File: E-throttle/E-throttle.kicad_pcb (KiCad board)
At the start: 2 copper layers, 100 x 100 mm, 49 parts, among them IC1 BTS441TG, J1 Micro_SD_Card_Det1, J3 Conn_01x11, J4 Conn_01x11, J5 776087-1, Q1 NMOS, SW1 SW_Push, U1 74HC123, U2 LM317_SOT-223, U3 LM317_SOT-223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

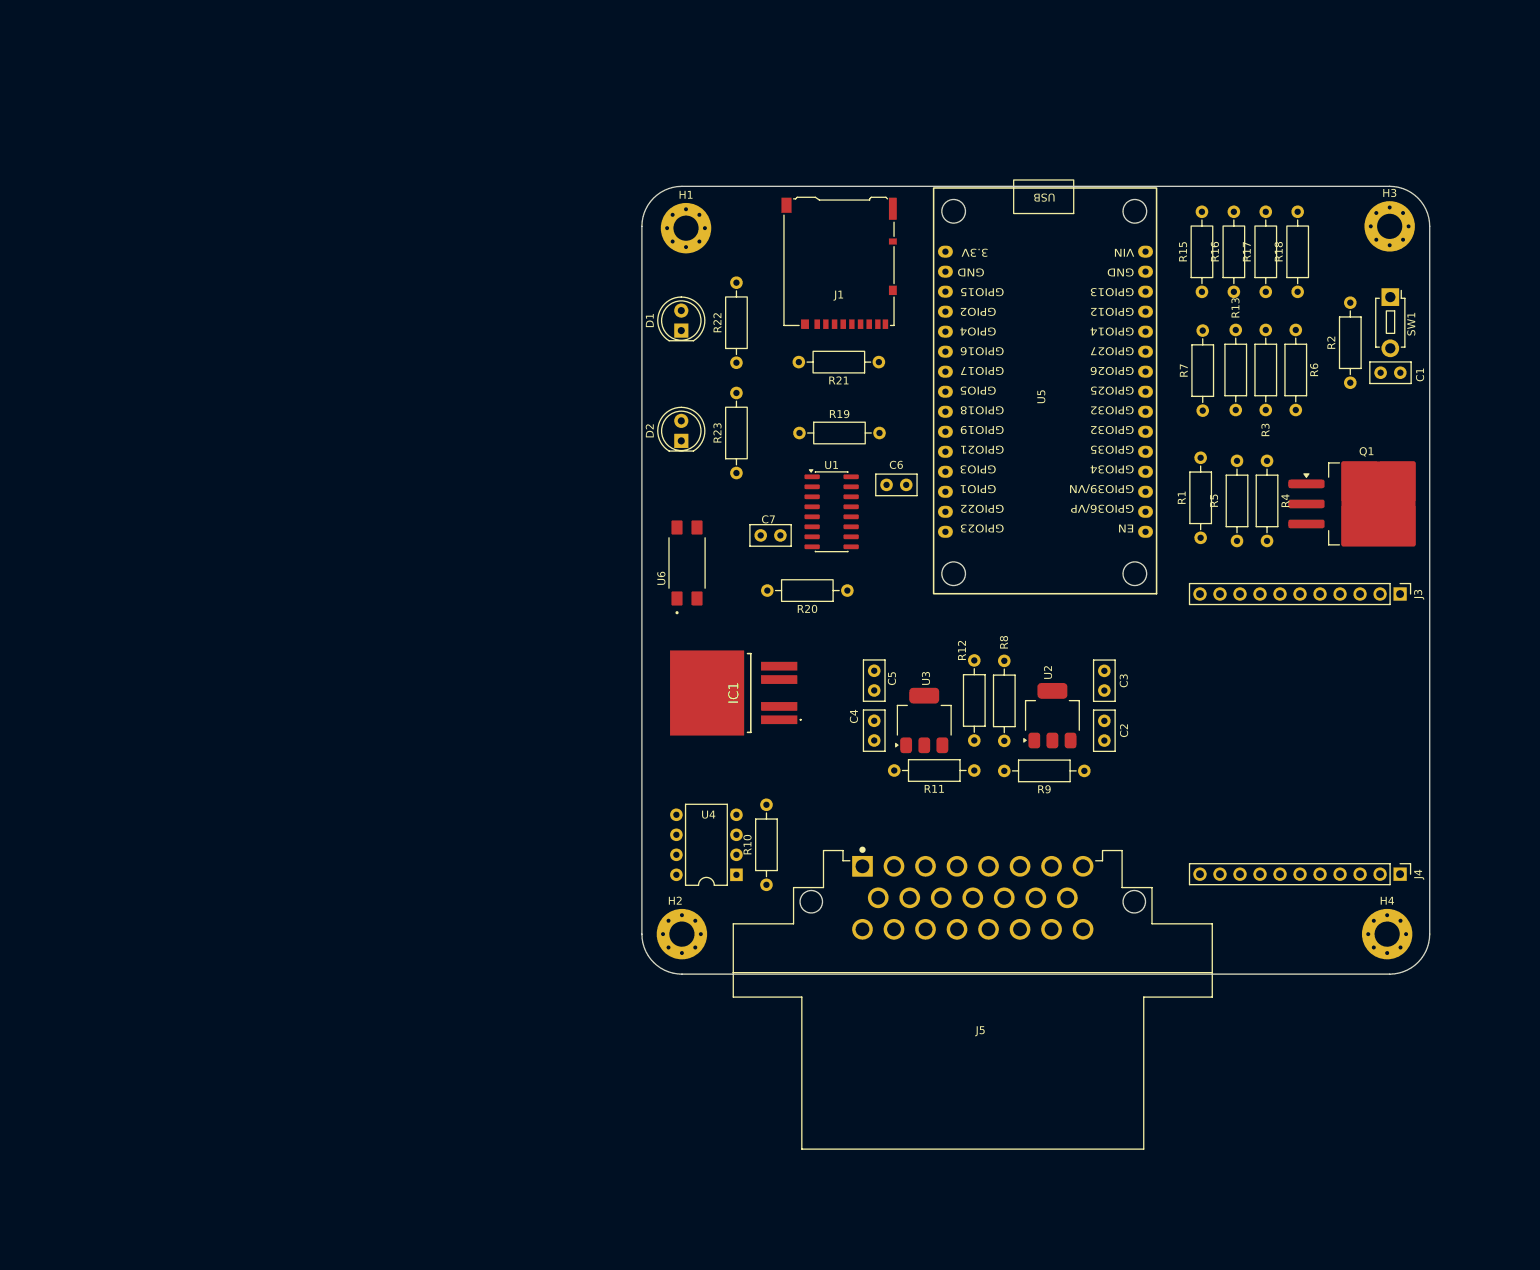
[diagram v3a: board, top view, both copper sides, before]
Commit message: Adjusted layout, added ground plane
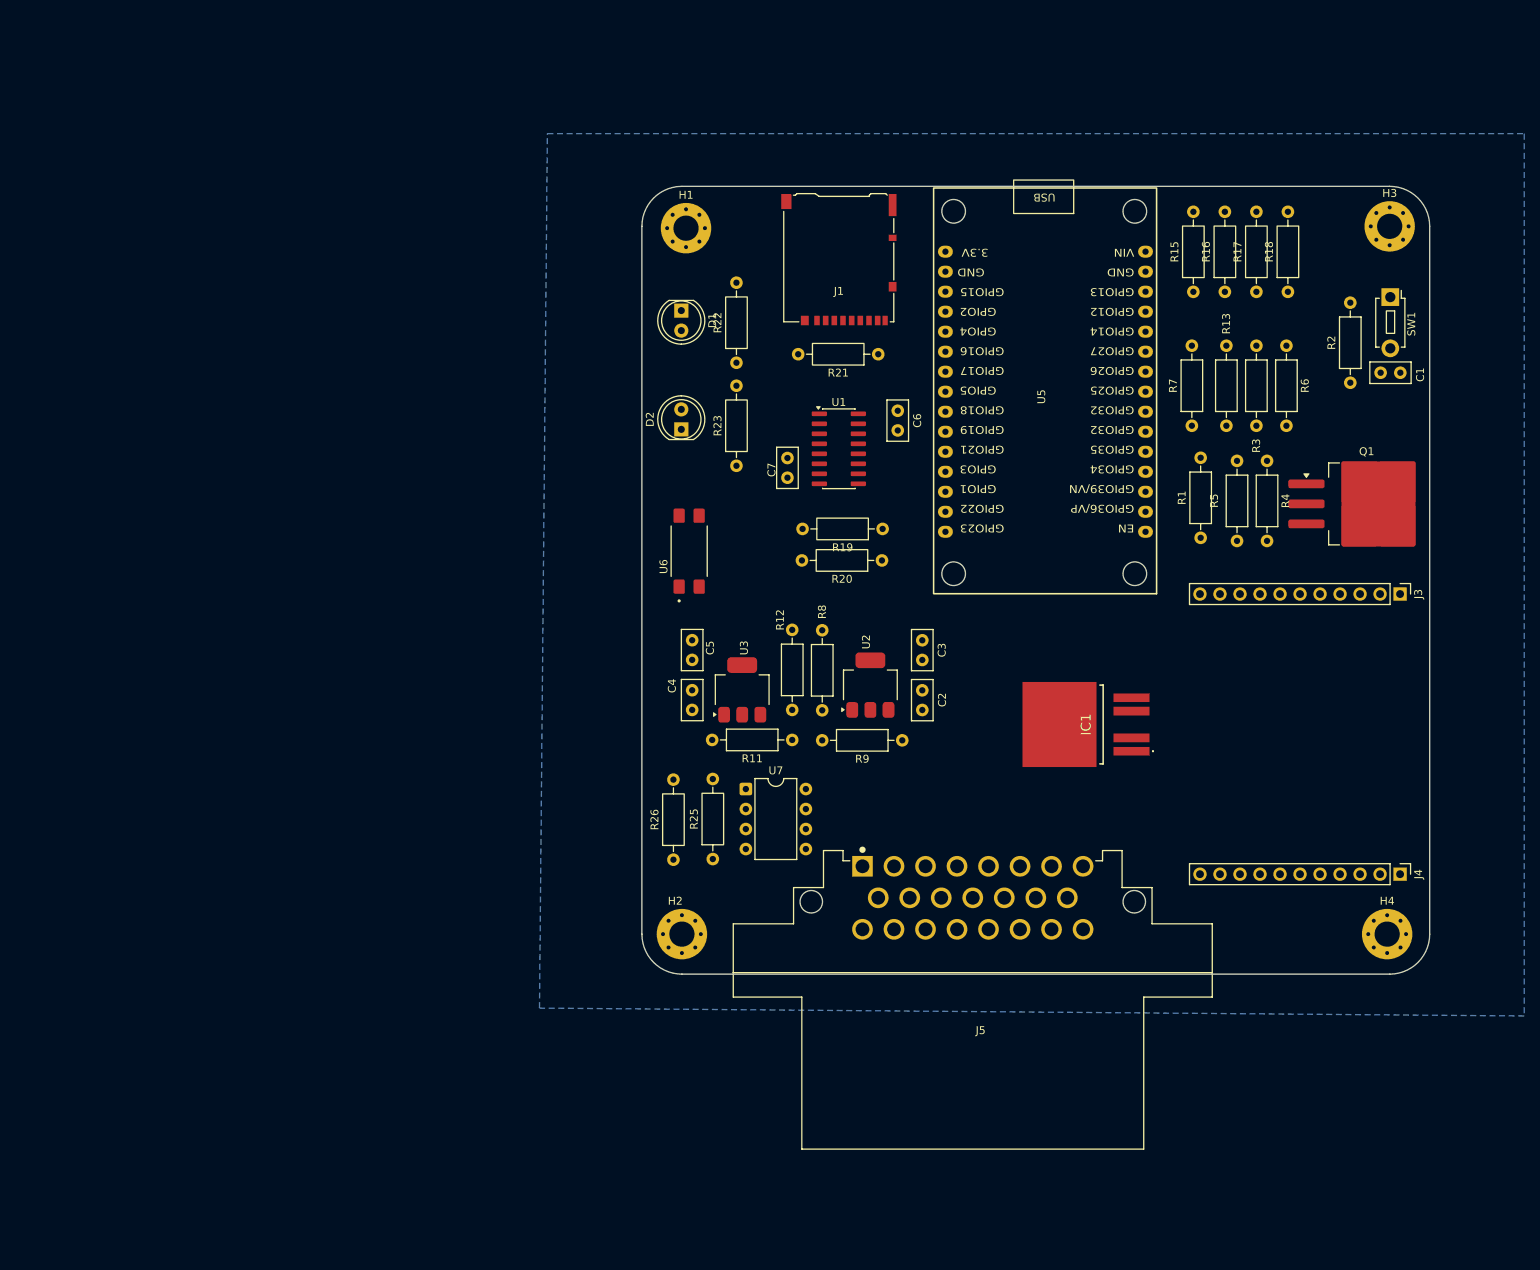
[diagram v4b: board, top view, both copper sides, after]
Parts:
- removed R10: 20k, Resistor_THT:R_Axial_DIN0207_L6.3mm_D2.5mm_P10.16mm_Horizontal
- removed U4: MCP2551-I-P, Package_DIP:DIP-8_W7.62mm
- added R25: 33.2k, Resistor_THT:R_Axial_DIN0207_L6.3mm_D2.5mm_P10.16mm_Horizontal, F.Cu at (163.7, 118.9)
- added R26: 66.5k, Resistor_THT:R_Axial_DIN0207_L6.3mm_D2.5mm_P10.16mm_Horizontal, F.Cu at (158.7, 119.0)
- added U7: MCP2561-E-P, Package_DIP:DIP-8_W7.62mm, F.Cu at (167.9, 110.0)
- moved IC1 44.9 mm to (210.4, 101.8)
- moved C4 23.4 mm to (161.1, 97.5)
- moved C5 23.4 mm to (161.1, 91.1)
- moved U2 23.4 mm to (183.7, 96.8)
- moved U3 23.4 mm to (167.4, 97.4)
- moved C2 23.4 mm to (190.3, 100.0)
- moved C3 23.4 mm to (190.3, 91.1)
- moved R11 23.4 mm to (173.8, 103.8)
- moved R12 23.4 mm to (173.8, 100.0)
- moved R8 23.4 mm to (177.6, 100.0)
- moved R9 23.4 mm to (187.8, 103.8)
- moved R19 16.1 mm to (185.3, 77.0), turned to 180 degrees
- moved C6 9.52 mm to (187.2, 62.0), turned to -90 degrees
- moved C7 8.07 mm to (173.2, 70.5), turned to 90 degrees
- moved U1 8.05 mm to (179.7, 66.8)
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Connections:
- U5 pad 10: /TPS-SIG1-OUT -> /APPS-SIG2-OUT
- U5 pad 20: unconnected-(U5-D4-Pad20) -> /IDLE
- U5 pad 21: /IDLE -> /CAN-RX-OUT
- U5 pad 22: /BLIP-OUT -> /CAN-TX
- U5 pad 7: unconnected-(U5-D26-Pad7) -> /BLIP-OUT
- U5 pad 9: /APPS-SIG2-OUT -> /TPS-SIG1-OUT
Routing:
- added copper zone on B.Cu, net GND

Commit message: arranged components
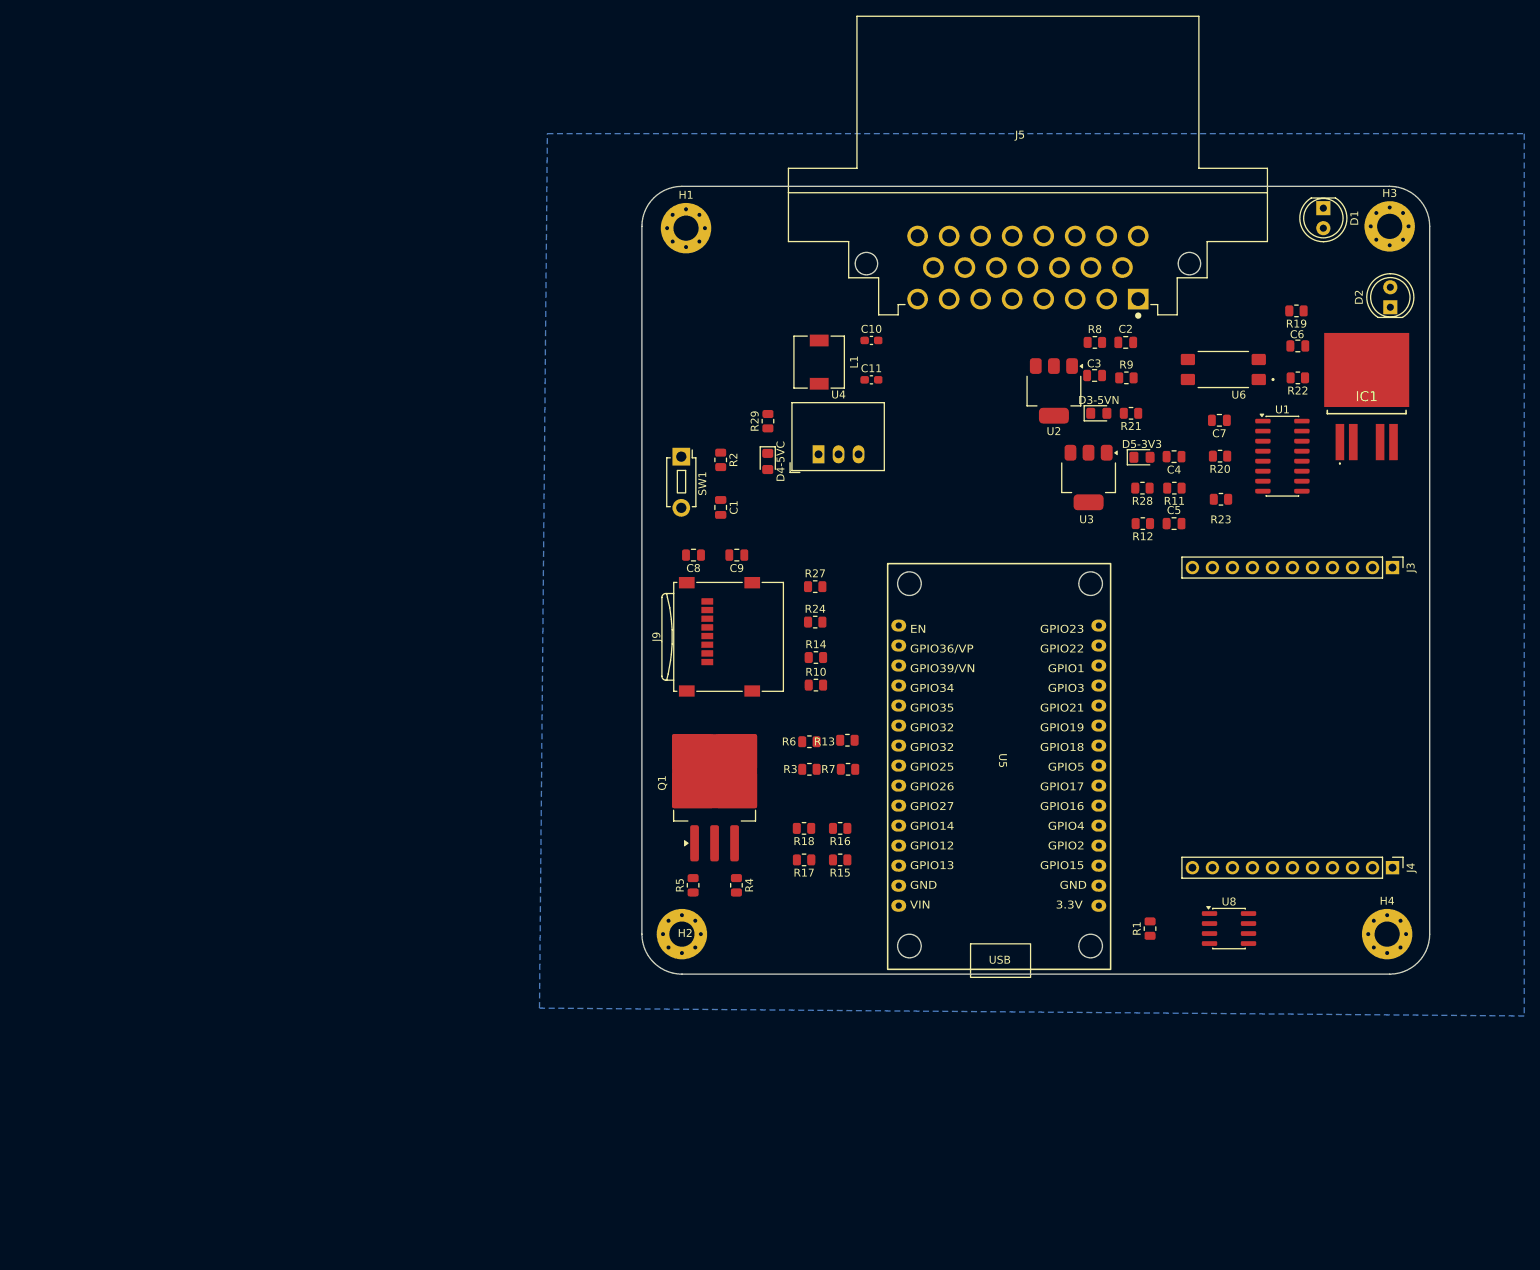
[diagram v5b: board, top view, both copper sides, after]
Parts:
- removed G***: LOGO, FBR_Footprints:FBR_Logo_.9in
- removed J1: Micro_SD_Card_Det1, Connector_Card:microSD_HC_Hirose_DM3AT-SF-PEJM5
- removed R25: 33.2k, Resistor_THT:R_Axial_DIN0207_L6.3mm_D2.5mm_P10.16mm_Horizontal
- removed R26: 66.5k, Resistor_THT:R_Axial_DIN0207_L6.3mm_D2.5mm_P10.16mm_Horizontal
- removed U7: MCP2561-E-P, Package_DIP:DIP-8_W7.62mm
- added C10: 10u, Capacitor_SMD:C_0603_1608Metric_Pad1.08x0.95mm_HandSolder, F.Cu at (183.9, 53.1)
- added C11: 4.7u, Capacitor_SMD:C_0603_1608Metric_Pad1.08x0.95mm_HandSolder, F.Cu at (183.9, 58.1)
- added C8: 100n, Capacitor_SMD:C_0805_2012Metric, F.Cu at (161.3, 80.3)
- added C9: 10u, Capacitor_SMD:C_0805_2012Metric, F.Cu at (166.8, 80.3)
- added D3-5VN: LED, LED_SMD:LED_0805_2012Metric_Pad1.15x1.40mm_HandSolder, F.Cu at (212.7, 62.3)
- added D4-5VC: LED, LED_SMD:LED_0805_2012Metric_Pad1.15x1.40mm_HandSolder, F.Cu at (170.7, 68.4)
- added D5-3V3: LED, LED_SMD:LED_0805_2012Metric_Pad1.15x1.40mm_HandSolder, F.Cu at (218.2, 67.9)
- added J9: Micro_SD_Card, Connector_Card:microSD_HC_Wuerth_693072010801, F.Cu at (164.6, 90.7)
- added L1: 12u, Inductor_SMD:L_6.3x6.3_H3, F.Cu at (177.2, 55.8)
- added R10: 10k, Resistor_SMD:R_0805_2012Metric, F.Cu at (176.8, 96.8)
- added R14: 10k, Resistor_SMD:R_0805_2012Metric, F.Cu at (176.8, 93.3)
- added R24: 10k, Resistor_SMD:R_0805_2012Metric, F.Cu at (176.7, 88.8)
- added R27: 10k, Resistor_SMD:R_0805_2012Metric, F.Cu at (176.7, 84.3)
- added R28: 100, Resistor_SMD:R_0805_2012Metric, F.Cu at (218.3, 71.8)
- added R29: 220, Resistor_SMD:R_0805_2012Metric, F.Cu at (170.7, 63.3)
- added U4: R-78E5.0-0.5, Converter_DCDC:Converter_DCDC_RECOM_R-78E-0.5_THT, F.Cu at (177.1, 67.5)
- added U8: SN65HVD230, Package_SO:SOIC-8_3.9x4.9mm_P1.27mm, F.Cu at (229.2, 127.7)
- C1, C2, C3, C4, C5, C6, C7: footprint Capacitor_THT:C_Disc_D5.0mm_W2.5mm_P2.50mm -> Capacitor_SMD:C_0805_2012Metric
- R1, R11, R12, R13, R15, R16, R17, R18, R2, R20, R22, R23, R3, R4, R5, R6, R7, R8, R9: footprint Resistor_THT:R_Axial_DIN0207_L6.3mm_D2.5mm_P10.16mm_Horizontal -> Resistor_SMD:R_0805_2012Metric
- R19: value 100k -> 10k; footprint Resistor_THT:R_Axial_DIN0207_L6.3mm_D2.5mm_P10.16mm_Horizontal -> Resistor_SMD:R_0805_2012Metric
- R21: value 10k -> 220; footprint Resistor_THT:R_Axial_DIN0207_L6.3mm_D2.5mm_P10.16mm_Horizontal -> Resistor_SMD:R_0805_2012Metric
- moved SW1 92.2 mm to (159.7, 67.8)
- moved R17 92.2 mm to (175.3, 119.0), turned to 180 degrees
- moved R18 91.7 mm to (175.3, 115.0), turned to 180 degrees
- moved D2 91.3 mm to (249.7, 48.9)
- moved Q1 90.0 mm to (163.9, 109.2), turned to 90 degrees
- moved R4 86.2 mm to (166.7, 122.2)
- moved C1 85.5 mm to (164.7, 74.3), turned to -90 degrees
- moved R15 84.9 mm to (179.9, 119.0), turned to 180 degrees
- moved R16 83.8 mm to (179.9, 115.0), turned to 180 degrees
- moved D1 82.5 mm to (241.2, 36.3)
- moved R5 81.7 mm to (161.2, 122.2)
- moved R2 80.5 mm to (164.7, 68.2), turned to -90 degrees
- moved J5 80.3 mm to (203.7, 43.8), turned to 180 degrees
- moved R6 78.7 mm to (176.0, 104.0), turned to 0 degrees
- moved U6 71.6 mm to (228.5, 56.8), turned to 180 degrees
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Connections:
- C3 pad 1: +5V -> +5V-SENSORS
- C4 pad 1: +12V -> +5V
- J5 pad 11: +5V -> +5V-SENSORS
- J5 pad 5: +5V -> +5V-SENSORS
- J5 pad 8: +5V -> +5V-SENSORS
- R21 pad 1: /CARD-DETECT -> Net-(D3-K)
- R21 pad 2: +3V3 -> GND
- R9 pad 1: +5V -> +5V-SENSORS
- U2 pad 2: +5V -> +5V-SENSORS
- U3 pad 3: +12V -> +5V
- U5 pad 21: /CAN-RX-OUT -> /CAN-TX
- U5 pad 22: /CAN-TX -> /CAN-RX
- U5 pad 29: /CARD-DETECT -> unconnected-(U5-D22/SCL-Pad29)
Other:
- board text removed: "Designed by Samuel Liu and Clement Tong, Mar 2026"
